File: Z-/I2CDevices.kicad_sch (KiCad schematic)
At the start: 43 parts, among them Q20 IRLML2803, Q21 SiRA99DP, U1 OPT4003DNPRQ1, U2 PCA9633DP2, U3 ADM1176-1ARMZ-R7, U4 DRV8235RTER

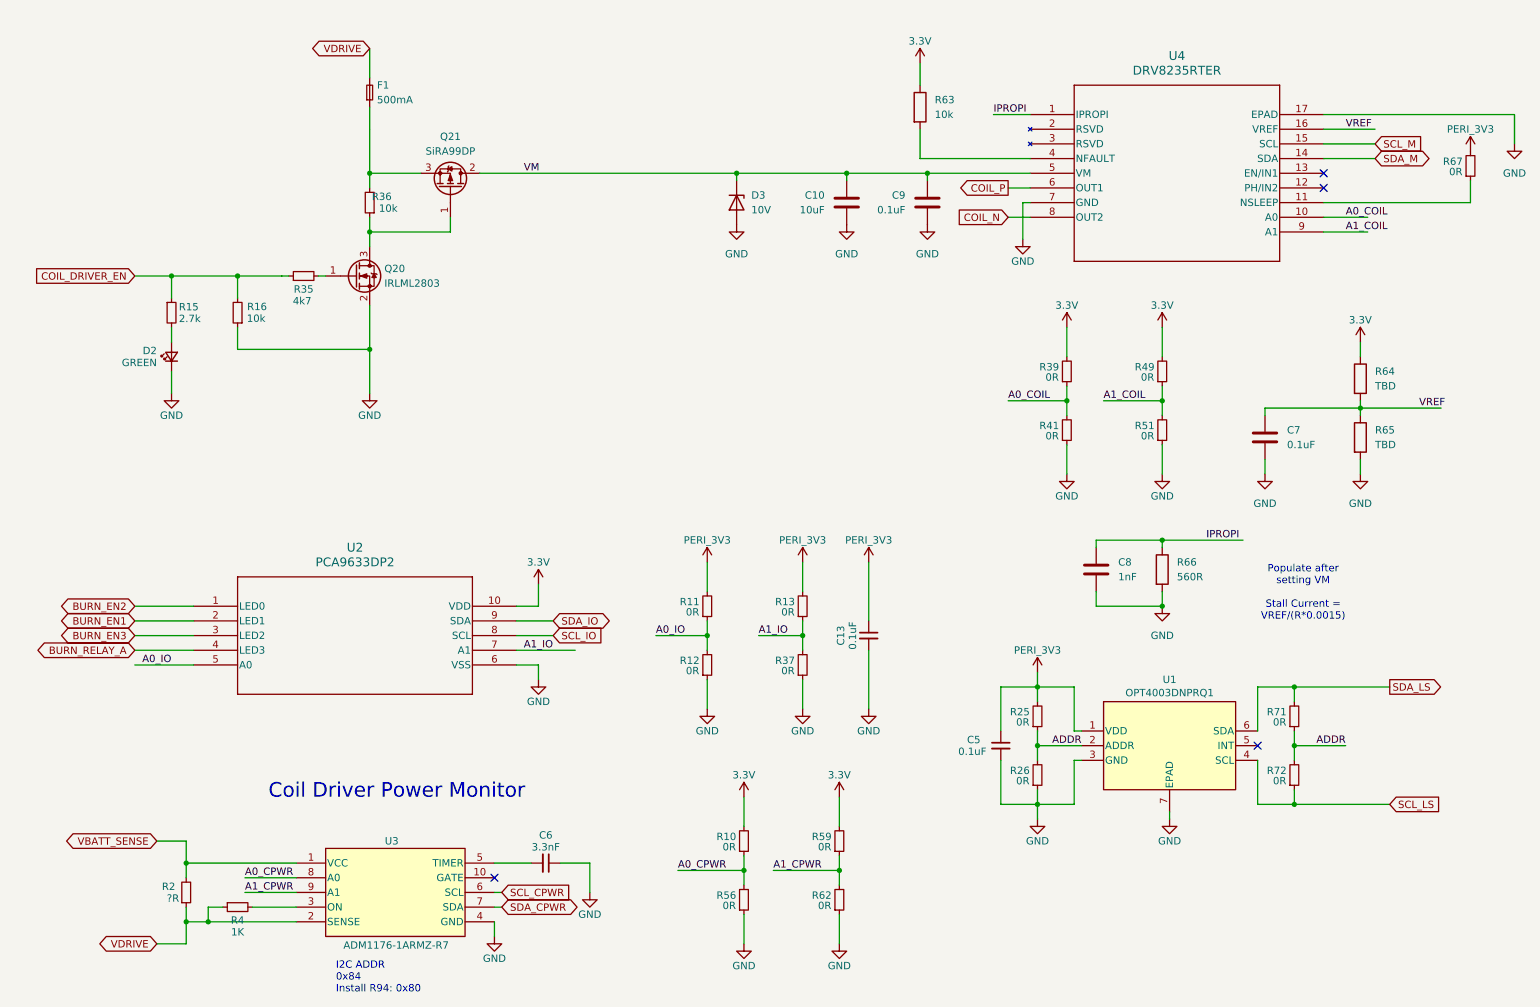
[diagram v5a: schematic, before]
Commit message: Updated schematics/layout with mainboard compatability
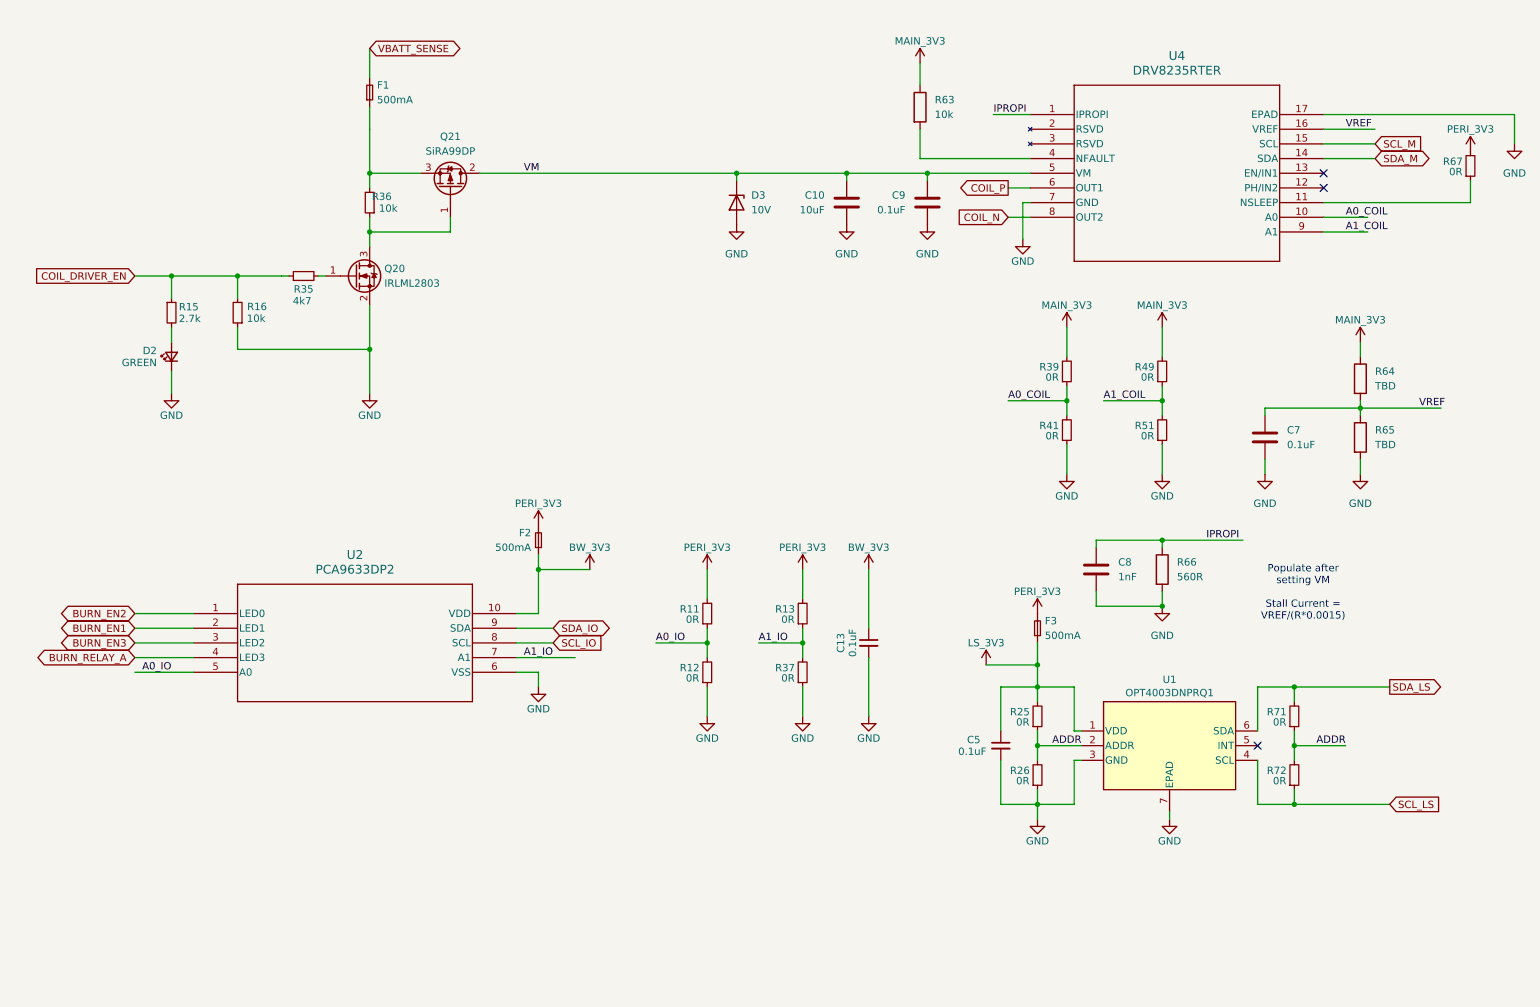
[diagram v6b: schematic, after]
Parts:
- removed C6: 3.3nF, Capacitor_SMD:C_0603_1608Metric, symbol Device:C_Small
- removed R10, R56, R59, R62: 0R, Resistor_SMD:R_0603_1608Metric, symbol Device:R_Small
- removed R2: ?R, Resistor_SMD:R_2512_6332Metric, symbol Device:R_Small
- removed R4: 1K, Resistor_SMD:R_0603_1608Metric, symbol Device:R_Small
- removed U3: ADM1176-1ARMZ-R7, Package_SO:MSOP-10_3x3mm_P0.5mm, symbol Argus-IC:ADM1176-1ARMZ-R7
- added F2, F3: 500mA, Fuse:Fuse_0603_1608Metric, symbol Device:Fuse_Small
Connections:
- net VDRIVE is gone; now on net VBATT_SENSE: F1.2
- net PERI_3V3: now also F2.2, F3.2; no longer C13.1, C5.1, R25.2, U1.1 (VDD)
- net 3.3V renamed MAIN_3V3
- net MAIN_3V3: no longer U2.10 (VDD)
- new net BW_3V3: C13.1, F2.1, U2.10 (VDD)
- new net LS_3V3: C5.1, F3.1, R25.2, U1.1 (VDD)
- no-connect marks 4 -> 3
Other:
- note removed: "Coil Driver Power Monitor"
- note removed: "I2C ADDR 0x84 Install R94: 0x80"
- moved on the sheet: C13, R11, R12, R13, R37, U2

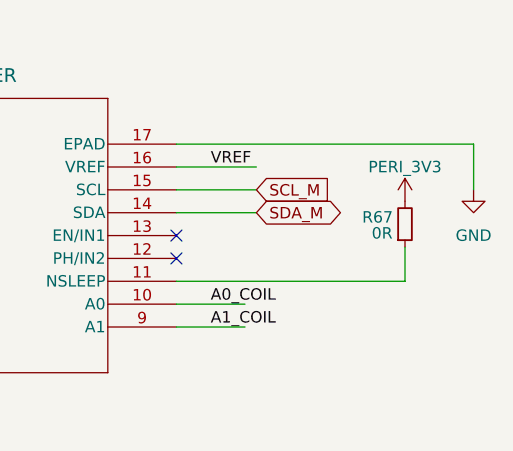
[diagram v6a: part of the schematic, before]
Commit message: Moved coil driver fully onto main 3v3
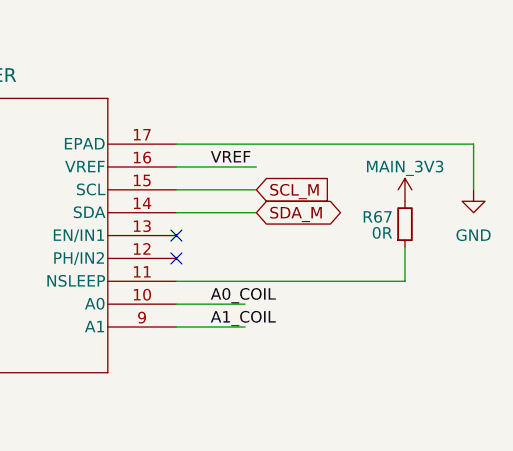
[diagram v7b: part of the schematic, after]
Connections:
- net MAIN_3V3: now also R67.2
- net PERI_3V3: no longer R67.2
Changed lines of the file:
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@@
 			)
 		)
-		(property "Value" "PERI_3V3"
+		(property "Value" "MAIN_3V3"
 			(at 267.97 39.37 0)
 			(effects
